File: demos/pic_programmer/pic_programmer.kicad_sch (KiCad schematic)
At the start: 56 parts, among them J1 DB9-FEMAL, P1 CONN_2, P101 CONN_1, P102 CONN_1, P103 CONN_1, P104 CONN_1, P105 CONN_1, P106 CONN_1, Q1 BC237, Q2 BC307, Q3 BC307, U2 74HC125, U3 7805, U4 LT1373

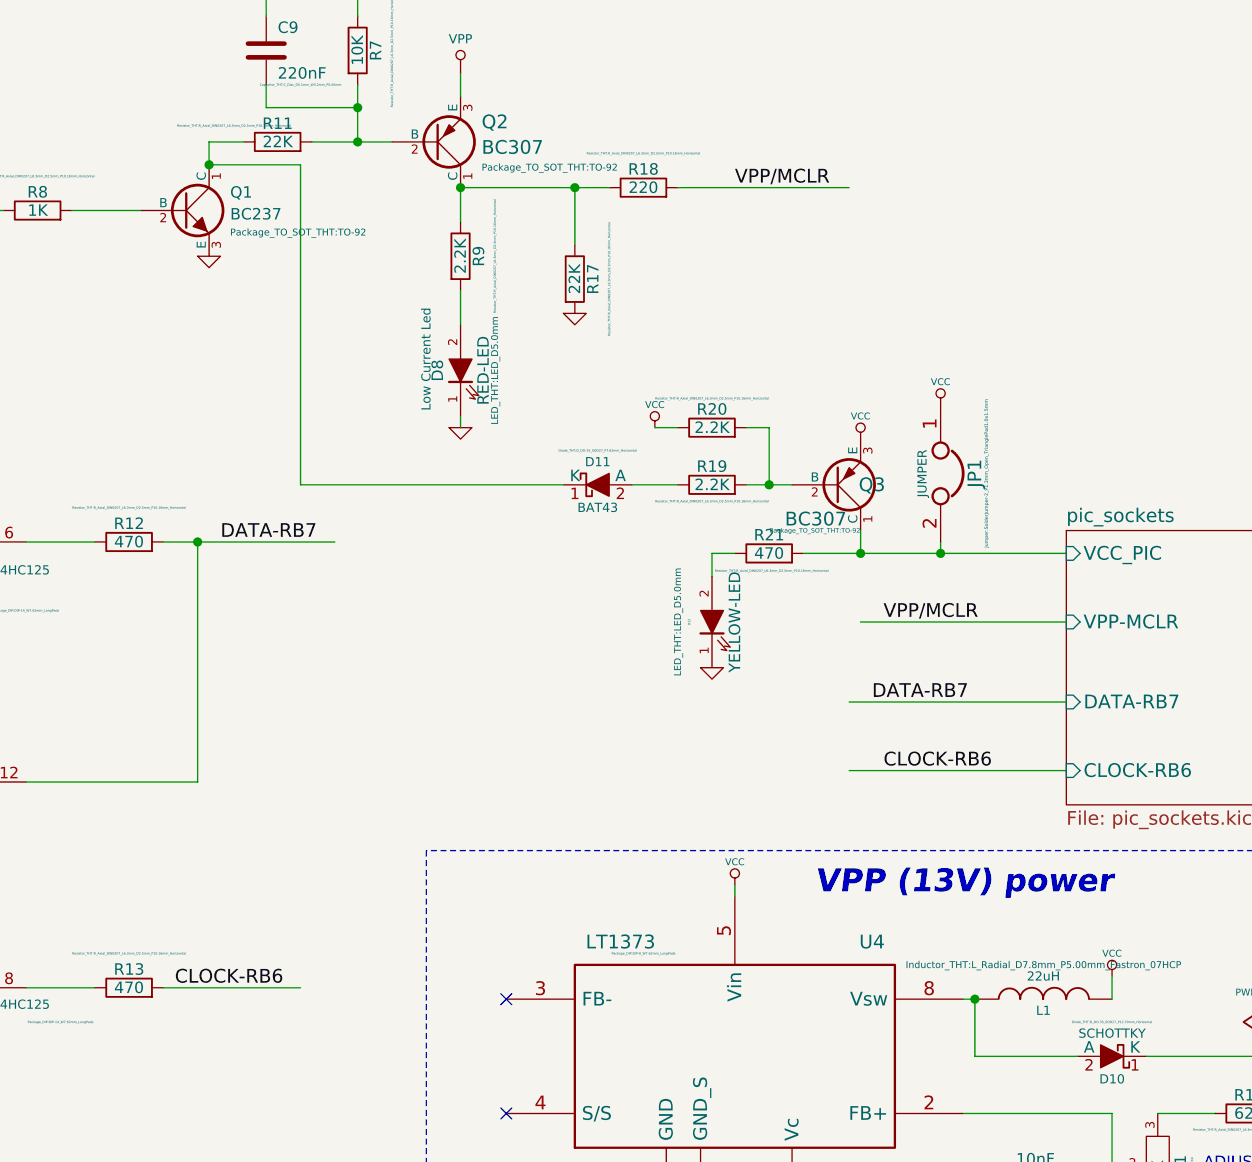
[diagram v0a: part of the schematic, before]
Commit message: feat: update kicad to 9.0.0+dfsg-1
Signed-off-by: lhdjply <lhdjply@126.com>
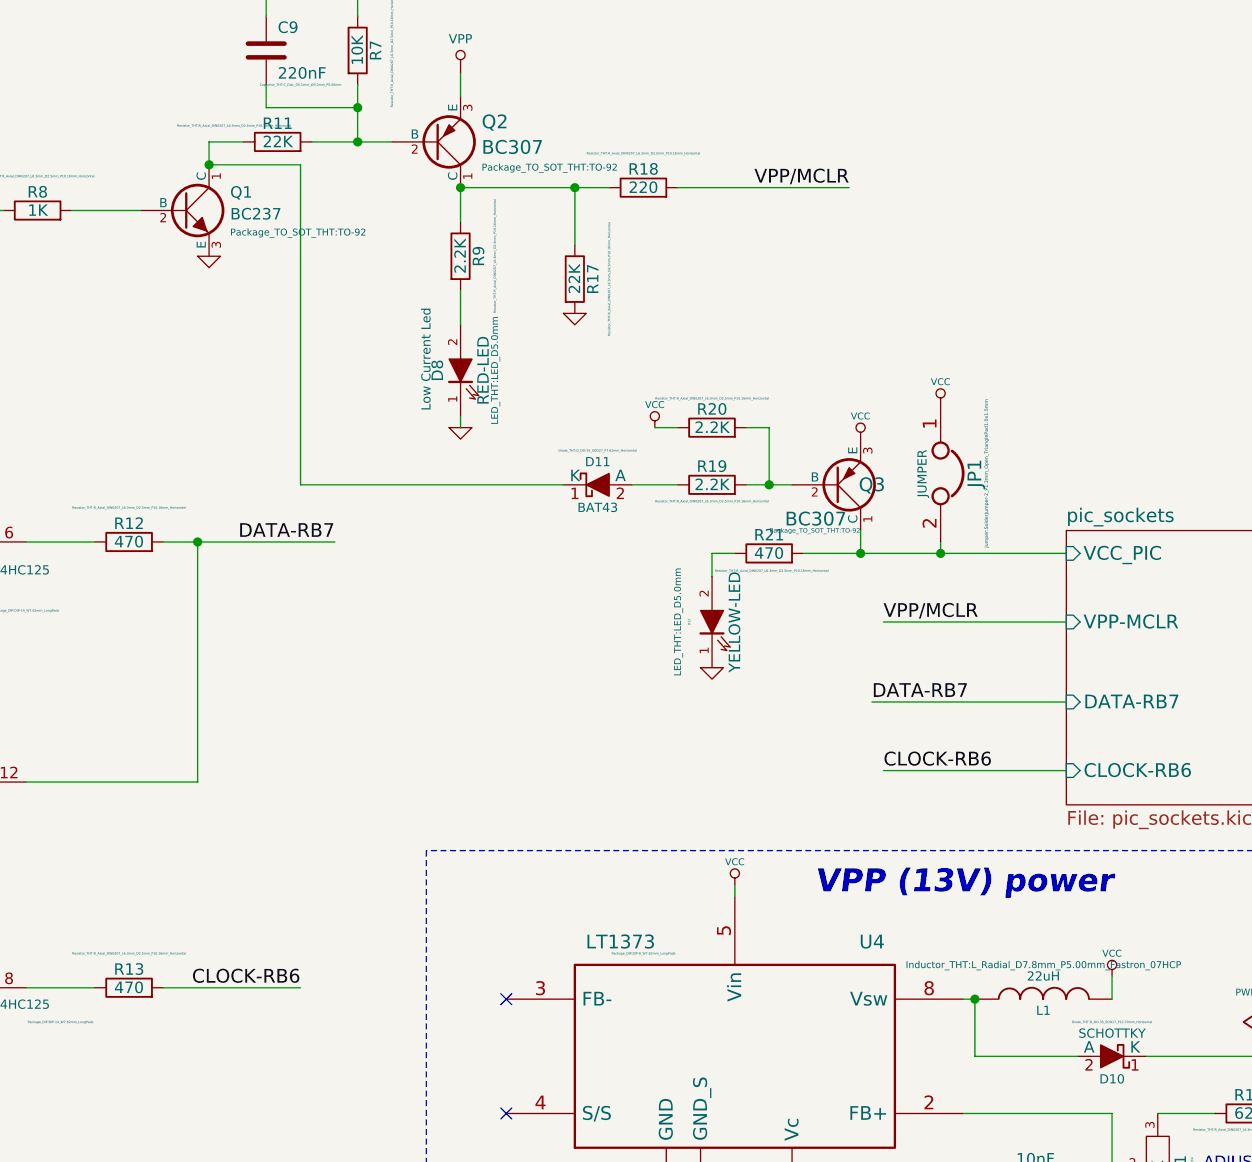
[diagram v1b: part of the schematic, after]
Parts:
- C1, C2, C3: symbol pic_programmer_schlib:CP -> pic_programmer:CP
- C4, C5, C9: symbol pic_programmer_schlib:C -> pic_programmer:C
- D1: symbol pic_programmer_schlib:D -> pic_programmer:D
- D10, D11, D2, D3, D4, D5, D6, D7: symbol pic_programmer_schlib:D_Schottky -> pic_programmer:D_Schottky
- D12, D8, D9: symbol pic_programmer_schlib:LED -> pic_programmer:LED
- J1: symbol pic_programmer_schlib:DB9 -> pic_programmer:DB9
- JP1: symbol pic_programmer_schlib:JUMPER -> pic_programmer:JUMPER
- L1: symbol pic_programmer_schlib:INDUCTOR -> pic_programmer:INDUCTOR
- P1: symbol pic_programmer_schlib:CONN_2 -> pic_programmer:CONN_2
- P101, P102, P103, P104, P105, P106: symbol pic_programmer_schlib:MOUNTING_HOLE -> pic_programmer:MOUNTING_HOLE
- Q1: symbol pic_programmer_schlib:BC237 -> pic_programmer:BC237
- Q2, Q3: symbol pic_programmer_schlib:BC307 -> pic_programmer:BC307
- R1, R10, R11, R12, R13, R14, R15, R16, R17, R18, R19, R2, R20, R21, R3, R4, R5, R6, R7, R8, R9: symbol pic_programmer_schlib:R -> pic_programmer:R
- RV1: symbol pic_programmer_schlib:POT -> pic_programmer:POT
- U2: symbol pic_programmer_schlib:74LS125 -> pic_programmer:74LS125
- U3: symbol pic_programmer_schlib:7805 -> pic_programmer:7805
- U4: symbol pic_programmer_schlib:LT1373 -> pic_programmer:LT1373
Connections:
- net VPP/MCLR: no longer R18.2
- new net VPP/MCLR: R18.2
